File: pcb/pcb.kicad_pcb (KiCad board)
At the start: 2 copper layers, 48 x 60 mm, 40 parts, among them J1 USB_C_Receptacle_USB2.0_14P, J3 LCD Data, J4 LCD CTRL, J5 MOISTURE, J6 HC-05, J7 DEBUG, J9 USART3 TX, SW1 PWR SWITCH, U1 TLV62569DBV, U2 STM32F446RETx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

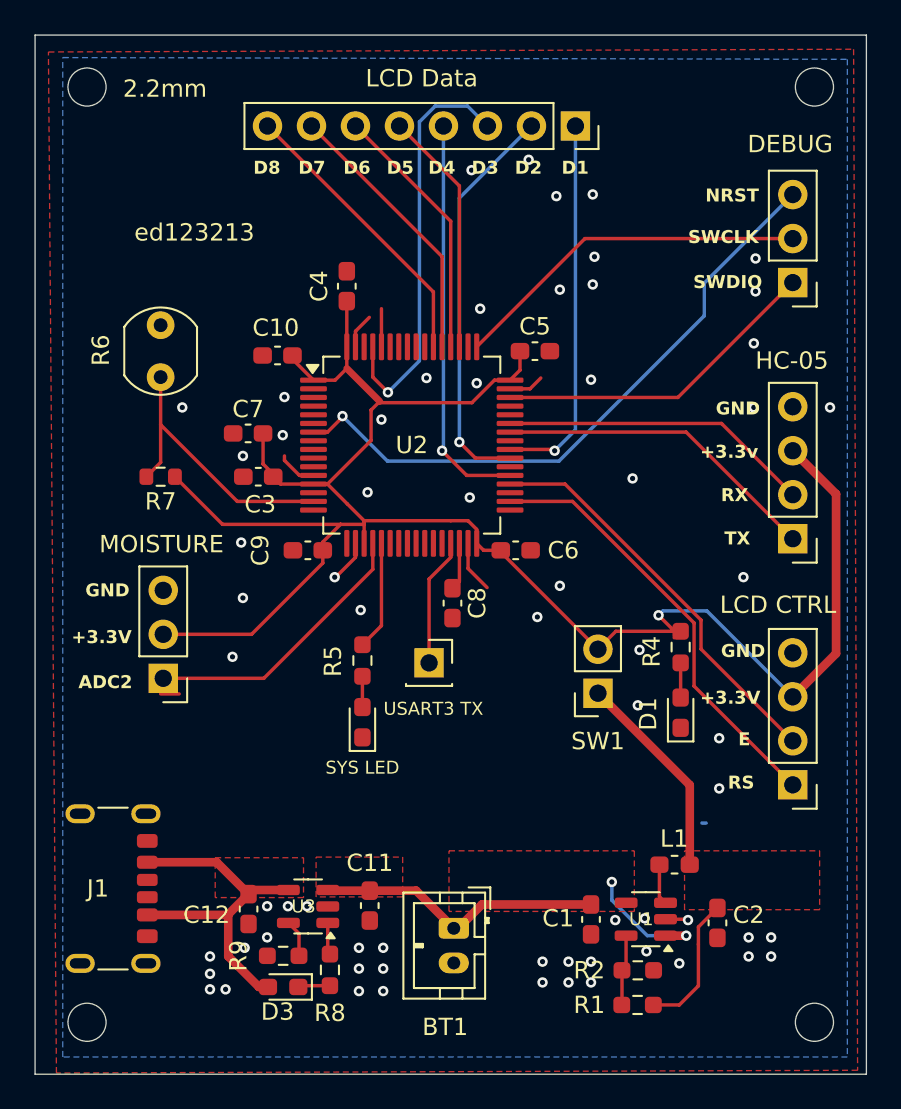
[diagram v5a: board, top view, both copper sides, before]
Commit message: start re-designing pcb
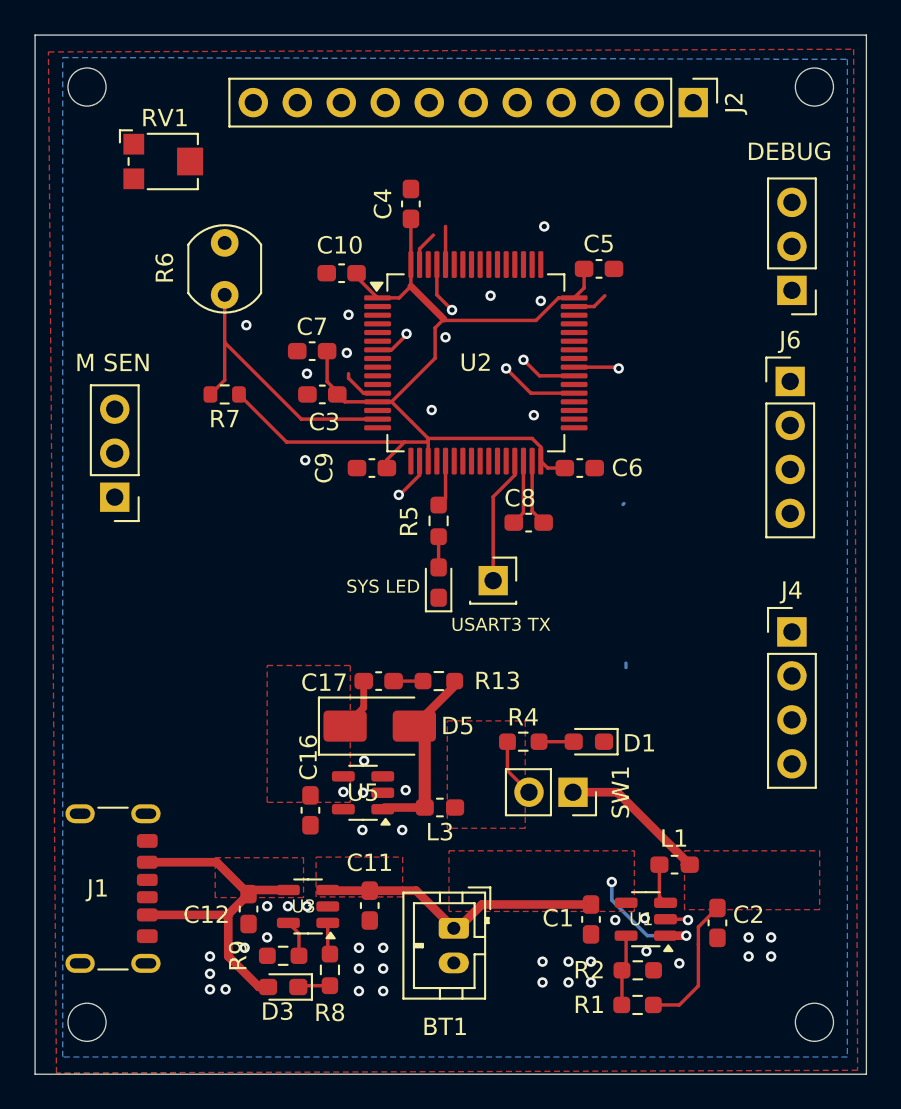
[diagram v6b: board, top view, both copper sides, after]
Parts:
- removed J3: LCD Data, Connector_PinSocket_2.54mm:PinSocket_1x08_P2.54mm_Vertical
- added C16: 22uF, Capacitor_SMD:C_0603_1608Metric_Pad1.08x0.95mm_HandSolder, F.Cu at (79.9, 84.3)
- added C17: 1nF, Capacitor_SMD:C_0603_1608Metric_Pad1.08x0.95mm_HandSolder, F.Cu at (83.8, 76.8)
- added D5: SS38, Diode_SMD:D_SMA, F.Cu at (83.9, 79.4)
- added J2: LCD, Connector_PinHeader_2.54mm:PinHeader_1x11_P2.54mm_Vertical, F.Cu at (102.0, 43.4)
- added L3: 2.2uH, Inductor_SMD:L_0603_1608Metric_Pad1.05x0.95mm_HandSolder, F.Cu at (87.4, 84.1)
- added R13: 10, Resistor_SMD:R_0603_1608Metric_Pad0.98x0.95mm_HandSolder, F.Cu at (87.3, 76.8)
- added RV1: LCD Contrast, Potentiometer_SMD:Potentiometer_Bourns_TC33X_Vertical, F.Cu at (71.5, 46.8)
- added U5: TPS613222ADBV, Package_TO_SOT_SMD:SOT-23-5, F.Cu at (82.9, 83.2)
- BT1: value 3.7v Li-ion -> 4.2v Lipo
- J5: value MOISTURE -> M SEN
- moved J5 10.8 mm to (68.6, 66.2)
- moved R4 10.6 mm to (92.2, 80.3), turned to 180 degrees
- moved D2 9.18 mm to (87.3, 71.1)
- moved R5 9.18 mm to (87.3, 67.5)
- moved J6 9.08 mm to (107.6, 59.5), turned to 0 degrees
- moved J4 8.83 mm to (107.7, 74.0), turned to 0 degrees
- moved C8 6.40 mm to (92.5, 67.7), turned to 0 degrees
- moved C10 6.02 mm to (81.7, 53.2)
- moved C3 6.02 mm to (80.6, 60.2)
- moved C4 6.02 mm to (85.7, 49.2)
- moved C5 6.02 mm to (96.6, 53.0)
- moved C6 6.02 mm to (95.5, 64.5)
- moved C7 6.02 mm to (80.0, 57.8)
- moved C9 6.02 mm to (83.5, 64.5)
- moved J9 6.02 mm to (90.5, 71.0)
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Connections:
- net +3.7V renamed +Vbat
- C12 pad 1: +5V -> +Vext
- C2 pad 1: +3.3V -> +3.3Vswin
- D3 pad 2: +5V -> +Vext
- J1 pad A9: +5V -> +Vext
- J1 pad B9: +5V -> +Vext
- J4 pad 3: +3.3V -> +5V
- J6 pad 3: +3.3V -> +5V
- L1 pad 2: +3.3V -> +3.3Vswin
- R1 pad 1: +3.3V -> +3.3Vswin
- R1 pad 2: +3.3V -> +3.3Vswin
- R2 pad 1: +3.3V -> +3.3Vswin
- SW1 pad 1: +3.3V -> +3.3Vswin
- U1 pad 5: +3.3V -> +3.3Vswin
- U3 pad 4: +5V -> +Vext
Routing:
- net +3.3V: track 137.6 -> 64.5 mm, vias 1 -> 0
- net NRST: track 36.7 -> 2.09 mm
- net LCD RS: track 25.2 -> 0.00 mm
- net LCD E: track 23.4 -> 0.00 mm
- net +Vext: track 0.00 -> 22.5 mm
- net +3.3Vswin: track 0.00 -> 21.3 mm
- net LCD D3: track 24.3 -> 3.16 mm
- net SWCLK: track 20.8 -> 0.00 mm
- net LCD D2: track 23.3 -> 3.31 mm
- net +5V: track 22.5 -> 3.05 mm
- net LCD D1: track 21.9 -> 2.61 mm
- net SWDIO: track 19.1 -> 0.00 mm
- net USART1 TX: track 18.9 -> 0.00 mm
- net LCD D4: track 23.3 -> 4.63 mm
- net USART1 RX: track 18.0 -> 0.00 mm
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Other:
- board text removed: "+3.3V"
- board text removed: "+3.3v"
- board text removed: "ADC2"
- board text removed: "D1"
- board text removed: "D2"
- board text removed: "D3"
- board text removed: "D4"
- board text removed: "D5"
- board text removed: "D6"
- board text removed: "D7"
- board text removed: "D8"
- board text removed: "E"
- board text removed: "GND"
- board text removed: "NRST"
- board text removed: "RS"
- board text removed: "RX"
- board text removed: "SWCLK"
- board text removed: "SWDIO"
- board text removed: "TX"
- board text removed: "ed123213"

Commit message: more pcb redesign
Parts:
- moved J6 7.78 mm to (107.6, 67.3), turned to 180 degrees
- moved J4 7.37 mm to (107.4, 81.3), turned to 180 degrees
- moved J5 6.31 mm to (71.4, 71.8)
- moved R6 4.18 mm to (71.4, 56.7)
- moved R7 3.65 mm to (71.4, 59.4)
- moved RV1 0.82 mm to (71.7, 47.6)
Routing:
- net +5V: track 3.05 -> 161.4 mm
- net NRST: track 2.09 -> 33.5 mm
- net +3.3V: track 64.5 -> 94.9 mm
- net LCD RS: track 0.00 -> 25.2 mm
- net LCD E: track 0.00 -> 23.7 mm
- net ADC2: track 0.00 -> 19.5 mm
- net LCD D2: track 3.31 -> 21.2 mm, vias 1 -> 2
- net LCD D4: track 4.63 -> 21.3 mm, vias 1 -> 2
- net LCD D3: track 3.16 -> 19.8 mm, vias 1 -> 0
- net USART1 TX: track 0.00 -> 16.5 mm
- net USART1 RX: track 0.00 -> 15.6 mm
- net SWCLK: track 0.00 -> 15.2 mm, vias 0 -> 1
- net SWDIO: track 0.00 -> 13.2 mm
- net LCD D8: track 0.00 -> 12.0 mm
- net LCD D7: track 0.00 -> 11.2 mm
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- added copper zone on F.Cu, net +3.3Vswin
- added copper zone on F.Cu, net +Vext
